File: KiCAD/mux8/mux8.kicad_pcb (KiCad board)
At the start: 4 copper layers, 17.8 x 30 mm, 12 parts, among them P1 CONN_02X07, P2 CONN_02X07, U1 MAX14662, U2 MAX14662, U3 PCF8574

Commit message: minor text changes to mux8 pcb
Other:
- board text added: "A0"
- board text added: "A1"
- board text added: "A2"
- board text added: "H"
- board text added: "L"
- board text added: "e924668"
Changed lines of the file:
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@@
     (area -4.30028 -15.384501 18.468001 15.075001)
     (thickness 1.6)
-    (drawings 4)
+    (drawings 14)
     (tracks 467)
     (zones 0)
@@
     (tags "resistor 0402")
     (attr smd)
-    (fp_text reference R1 (at -2.854368 0 180) (layer B.SilkS)
+    (fp_text reference R1 (at -2.854368 0 180) (layer B.SilkS) hide
       (effects (font (size 1 1) (thickness 0.15)) (justify mirror))
     )
@@
     (tags "resistor 0402")
     (attr smd)
-    (fp_text reference R2 (at 3.495632 0 180) (layer B.SilkS)
+    (fp_text reference R2 (at 3.495632 0 180) (layer B.SilkS) hide
       (effects (font (size 1 1) (thickness 0.15)) (justify mirror))
     )
@@
     (tags "resistor 0402")
     (attr smd)
-    (fp_text reference R3 (at -2.854368 0 180) (layer B.SilkS)
+    (fp_text reference R3 (at -2.854368 0 180) (layer B.SilkS) hide
       (effects (font (size 1 1) (thickness 0.15)) (justify mirror))
     )
@@
     (tags "resistor 0402")
     (attr smd)
-    (fp_text reference R4 (at 3.495632 0 180) (layer B.SilkS)
+    (fp_text reference R4 (at 3.495632 0 180) (layer B.SilkS) hide
       (effects (font (size 1 1) (thickness 0.15)) (justify mirror))
     )
@@
     (tags "resistor 0402")
     (attr smd)
-    (fp_text reference R5 (at -2.854368 0 180) (layer B.SilkS)
+    (fp_text reference R5 (at -2.854368 0 180) (layer B.SilkS) hide
       (effects (font (size 1 1) (thickness 0.15)) (justify mirror))
     )
@@
     (tags "resistor 0402")
     (attr smd)
-    (fp_text reference R6 (at 3.495632 0 180) (layer B.SilkS)
+    (fp_text reference R6 (at 3.495632 0 180) (layer B.SilkS) hide
       (effects (font (size 1 1) (thickness 0.15)) (justify mirror))
     )
@@
     (tags "QFN 0.4")
     (attr smd)
-    (fp_text reference U2 (at -0.45 1.2 180) (layer B.SilkS)
+    (fp_text reference U2 (at -1.6 3.19 180) (layer B.SilkS)
       (effects (font (size 1 1) (thickness 0.15)) (justify mirror))
     )
@@
     (tags "CMS SOJ")
     (attr smd)
-    (fp_text reference U3 (at -6.46 -5.08 -90) (layer B.SilkS)
+    (fp_text reference U3 (at -5.785 -5.34) (layer B.SilkS)
       (effects (font (size 1 1) (thickness 0.15)) (justify mirror))
     )
@@
     )
   )
+  (gr_text L (at 0.41 -10.62) (layer B.SilkS)
+    (effects (font (size 0.5 0.5) (thickness 0.125)) (justify mirror))
+  )
+  (gr_text H (at 5.5 -10.58) (layer B.SilkS)
+    (effects (font (size 0.5 0.5) (thickness 0.125)) (justify mirror))
+  )
+  (gr_text H (at 5.47 -13.12) (layer B.SilkS)
+    (effects (font (size 0.5 0.5) (thickness 0.125)) (justify mirror))
+  )
+  (gr_text L (at 0.4 -13.08) (layer B.SilkS)
+    (effects (font (size 0.5 0.5) (thickness 0.125)) (justify mirror))
+  )
+  (gr_text L (at 0.56 -7.22) (layer B.SilkS)
+    (effects (font (size 0.5 0.5) (thickness 0.125)) (justify mirror))
+  )
+  (gr_text H (at 5.5 -7.18) (layer B.SilkS)
+    (effects (font (size 0.5 0.5) (thickness 0.125)) (justify mirror))
+  )
+  (gr_text A2 (at 2.83 -14.22) (layer B.SilkS)
+    (effects (font (size 0.5 0.5) (thickness 0.125)) (justify mirror))
+  )
+  (gr_text A1 (at 2.94 -9.95) (layer B.SilkS)
+    (effects (font (size 0.5 0.5) (thickness 0.125)) (justify mirror))
+  )
+  (gr_text A0 (at 2.92 -6.37) (layer B.SilkS)
+    (effects (font (size 0.5 0.5) (thickness 0.125)) (justify mirror))
+  )
+  (gr_text e924668 (at 2 12.5 90) (layer B.SilkS)
+    (effects (font (size 0.5 0.5) (thickness 0.125)) (justify mirror))
+  )
   (gr_line (start 0 -15) (end 17.78 -15) (layer Edge.Cuts) (width 0.15))

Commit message: mux 8 done
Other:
- board text added: "78c87a6"
- board text removed: "e924668"
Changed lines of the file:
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@@
     (visible_elements FFFFFFFF)
     (pcbplotparams
-      (layerselection 0x00030_ffffffff)
+      (layerselection 0x010fc_ffffffff)
       (usegerberextensions false)
+      (usegerberattributes true)
       (excludeedgelayer true)
       (linewidth 0.150000)
@@
       (viasonmask false)
       (mode 1)
-      (useauxorigin false)
+      (useauxorigin true)
       (hpglpennumber 1)
       (hpglpenspeed 20)
@@
       (padsonsilk false)
       (subtractmaskfromsilk false)
-      (outputformat 3)
+      (outputformat 1)
       (mirror false)
       (drillshape 0)
@@
     (effects (font (size 0.5 0.5) (thickness 0.125)) (justify mirror))
   )
-  (gr_text e924668 (at 2 12.5 90) (layer B.SilkS)
+  (gr_text 78c87a6 (at 2 12.5 90) (layer B.SilkS)
     (effects (font (size 0.5 0.5) (thickness 0.125)) (justify mirror))
   )

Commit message: generate order packages
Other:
- board text added: "17e0726"
- board text removed: "78c87a6"
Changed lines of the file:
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@@
     (pcbplotparams
       (layerselection 0x010fc_ffffffff)
-      (usegerberextensions false)
+      (usegerberextensions true)
       (usegerberattributes true)
       (excludeedgelayer true)
@@
     (effects (font (size 0.5 0.5) (thickness 0.125)) (justify mirror))
   )
-  (gr_text 78c87a6 (at 2 12.5 90) (layer B.SilkS)
+  (gr_text 17e0726 (at 2 12.5 90) (layer B.SilkS)
     (effects (font (size 0.5 0.5) (thickness 0.125)) (justify mirror))
   )

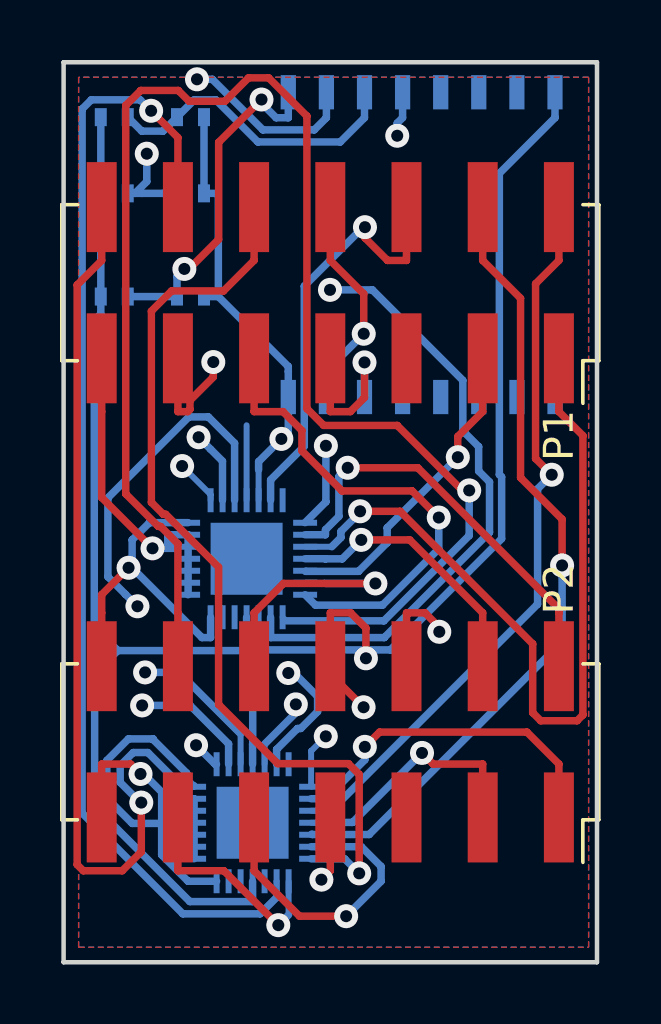
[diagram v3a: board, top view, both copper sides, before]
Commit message: fix pwr/gnd swap, fix extra clock signal name, fix pin hole sizes
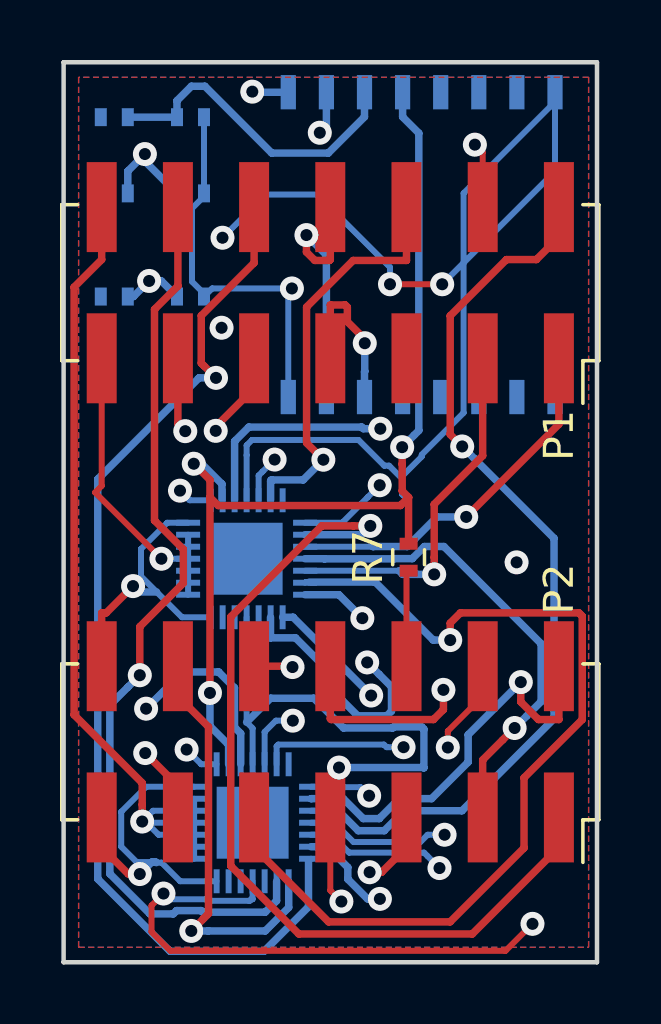
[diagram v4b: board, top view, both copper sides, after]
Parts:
- added R7: R, Resistors_SMD:R_0402, F.Cu at (11.5, 1.50)
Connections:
- P2 pad 1: L_V -> L_I
- P2 pad 10: 3_I -> 3_V
- P2 pad 11: 5_V -> 5_I
- P2 pad 12: 5_I -> 5_V
- P2 pad 2: L_I -> L_V
- P2 pad 3: 1_V -> 1_I
- P2 pad 4: 1_I -> 1_V
- P2 pad 5: SCK -> +3V3
- P2 pad 6: CLK -> SCK
- P2 pad 7: GND -> +5V
- P2 pad 8: +5V -> GND
- P2 pad 9: 3_V -> 3_I
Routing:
- net 5_V: track 51.9 -> 15.4 mm, vias 1 -> 2
- net 3_V: track 8.58 -> 31.4 mm
- net L_V: track 14.1 -> 30.6 mm
- net 0_V: track 26.4 -> 12.3 mm
- net GND: track 74.9 -> 83.5 mm, vias 2 -> 8
- net R_I: track 38.3 -> 30.9 mm
- net R_V: track 29.5 -> 22.5 mm
- net 1_V: track 8.97 -> 16.0 mm
- net SCK: track 32.1 -> 38.9 mm
- net 5_I: track 7.48 -> 13.9 mm
- net 0_I: track 24.4 -> 30.5 mm
- net MOSI: track 35.2 -> 29.4 mm
- net 2_I: track 26.6 -> 32.1 mm, vias 1 -> 2
- net I-: track 15.9 -> 11.0 mm
- net 4_I: track 30.7 -> 35.6 mm
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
